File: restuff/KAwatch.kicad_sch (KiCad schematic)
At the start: 23 parts, among them J1 Conn_01x08, J2 USB_C_Receptacle_PowerOnly_6P, J3 Conn_01x02, J4 Conn_01x02, Q1 Q_NPN_BCE, SW1 SW_Push, U1 ESP32-WROOM-32E, U2 MCP73831-2-OT, U3 AMS1117-3.3

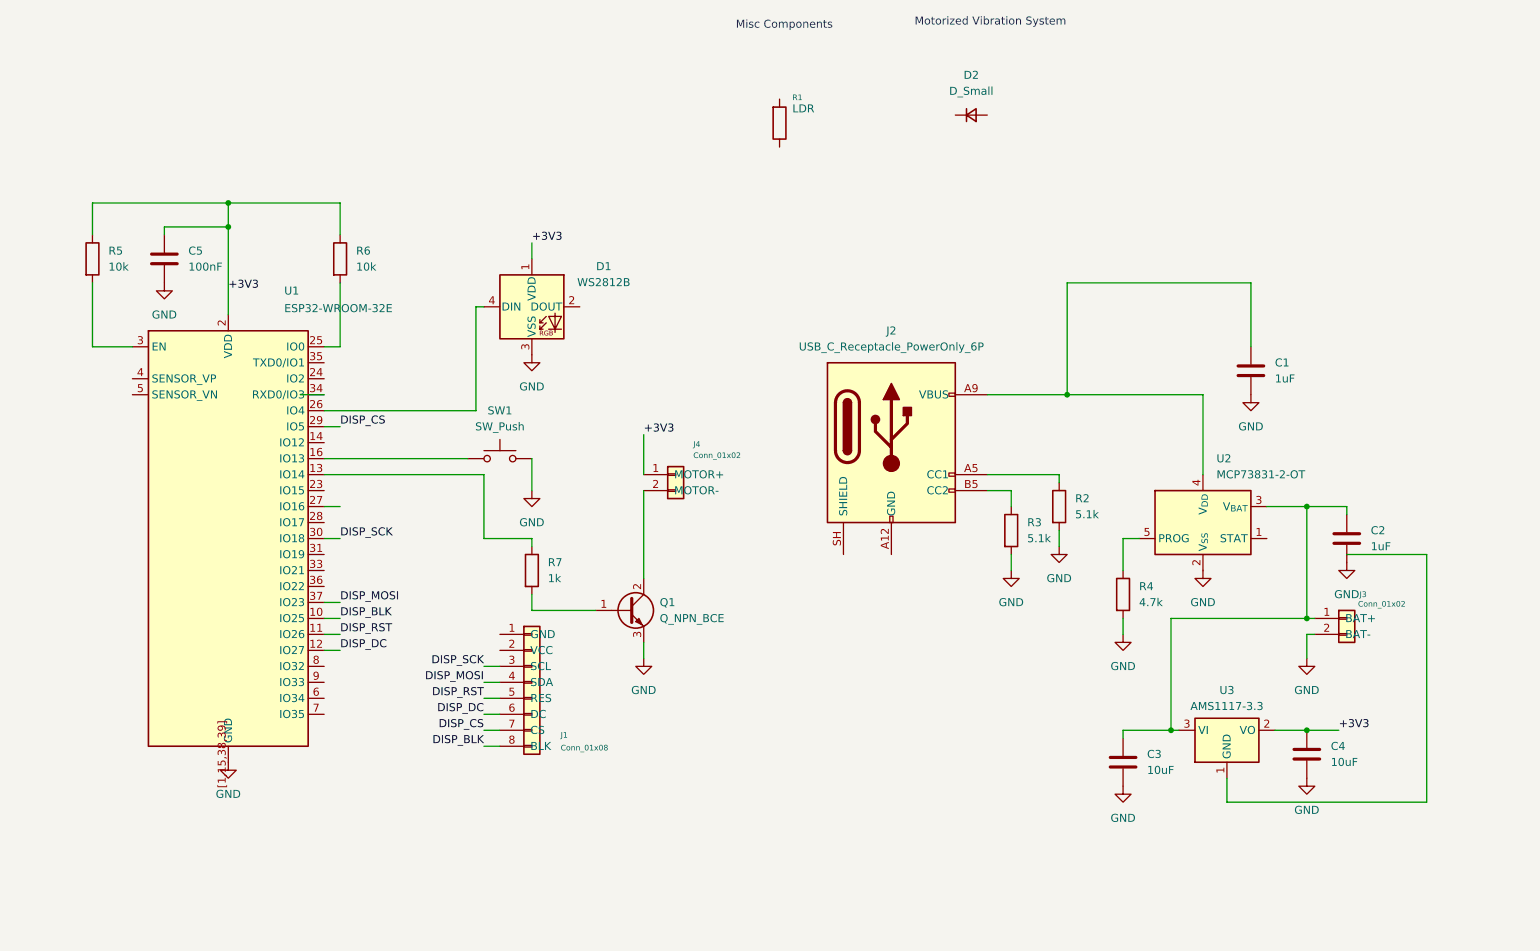
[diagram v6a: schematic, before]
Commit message: wiring op complete, ERC failure
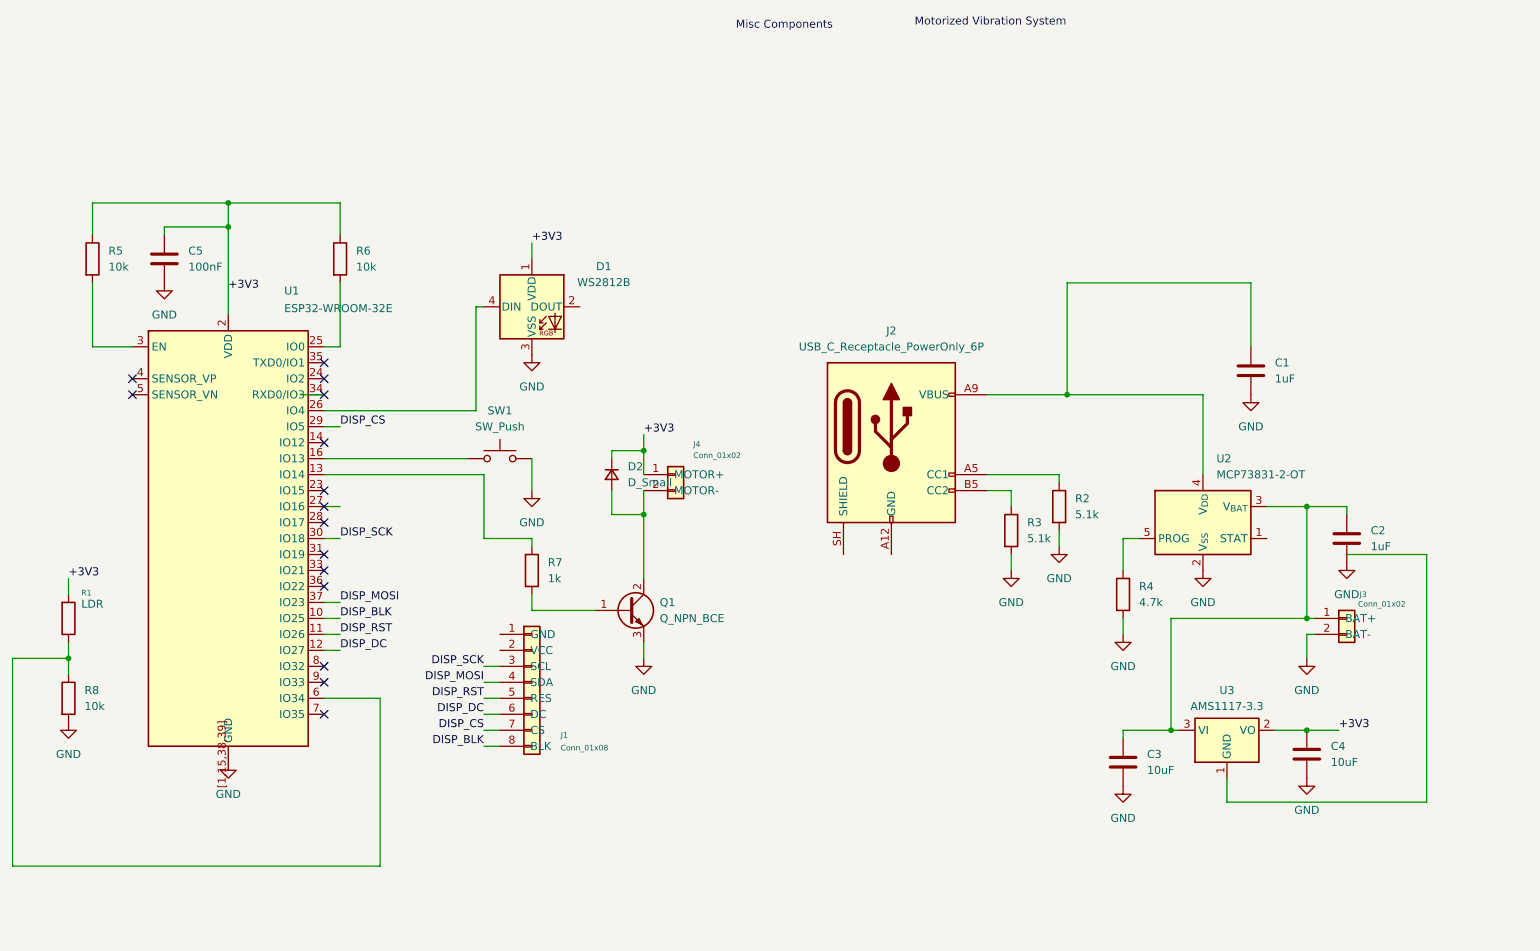
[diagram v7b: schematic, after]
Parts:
- added R8: 10k, symbol Device:R
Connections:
- net +3V3: now also D2.1 (K), R1.1
- net GND: now also R8.2
- net at R1.2: now also U1.6 (IO34), R8.1
- net at J4.2 (MOTOR-), Q1.2 (C): now also D2.2 (A)
- no-connect marks 0 -> 15
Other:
- moved on the sheet: D2, R1

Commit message: schematic W ERC complete
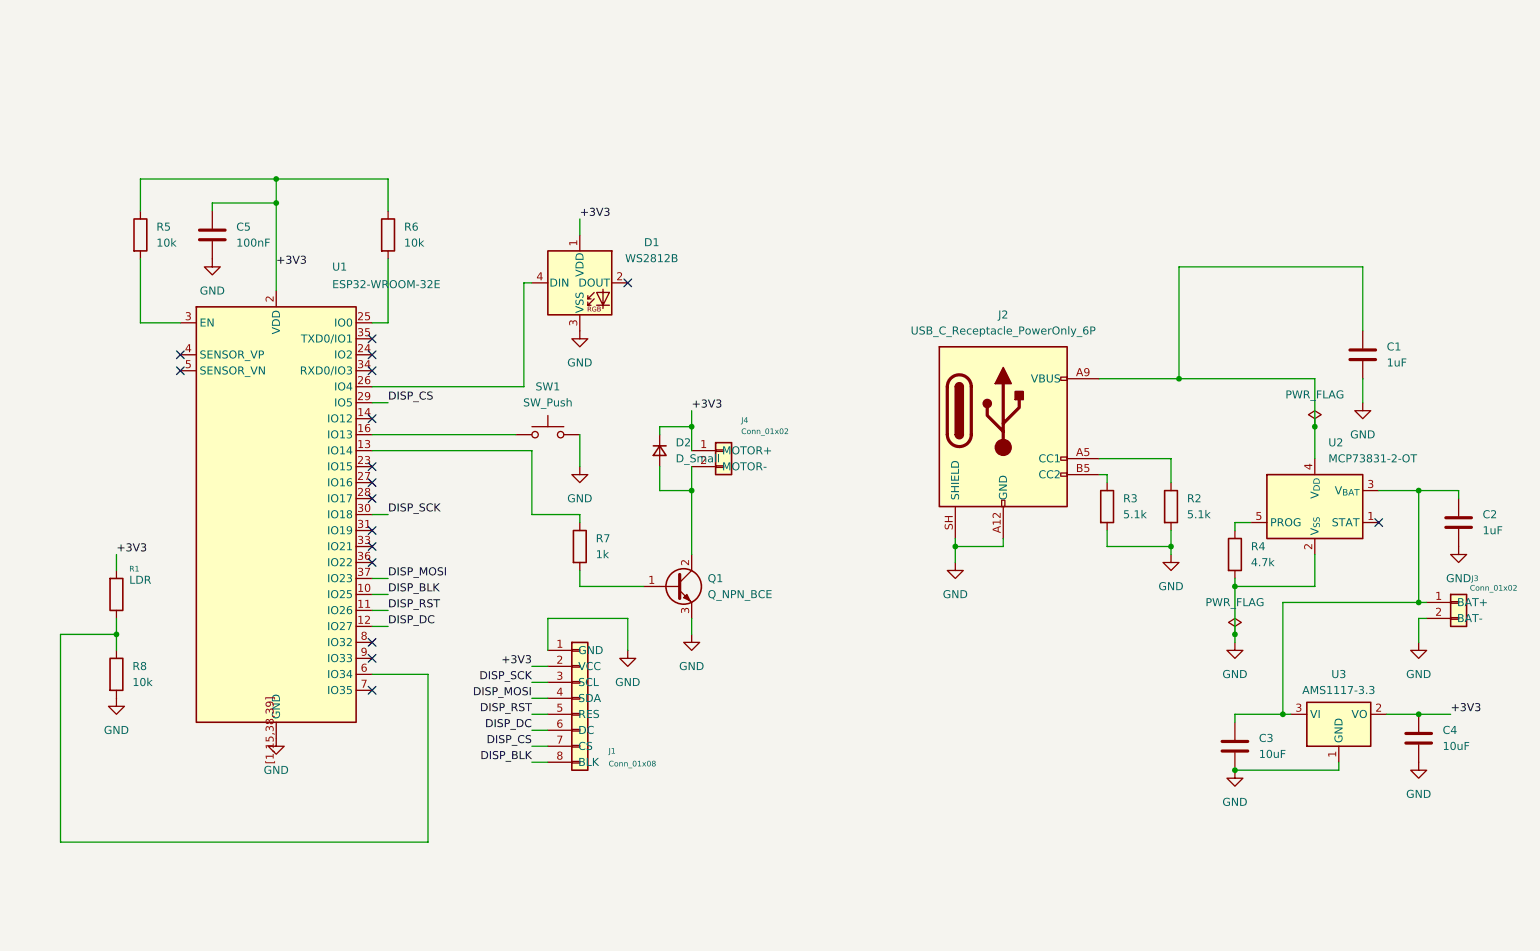
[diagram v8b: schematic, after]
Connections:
- net +3V3: now also J1.2 (VCC)
- net GND: now also J1.1 (GND), J2.A12 (GND), J2.B12 (GND), J2.SH (SHIELD), U3.1 (GND)
- no-connect marks 15 -> 17
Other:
- note removed: "Misc Components"
- note removed: "Motorized Vibration System"
- moved on the sheet: C1, C2, C3, C4, C5, D1, D2, J1, J2, J3, J4, Q1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
